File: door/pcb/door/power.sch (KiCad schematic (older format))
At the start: 6 parts, among them J1 USB_B_Micro, U1 LM1117-3.3

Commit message: caps voltage regulator gestauscht
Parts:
- removed C1: 10uF, Capacitor_SMD:C_0805_2012Metric, symbol Device:C
- removed C2: 100uF, Capacitor_SMD:C_0805_2012Metric, symbol Device:C
- added C1, C2: 10uF, Capacitor_Tantalum_SMD:CP_EIA-3216-10_Kemet-I, symbol Device:CP
- J1: footprint Connector_USB:USB_Micro-B_Amphenol_10103594-0001LF_Horizontal -> Connector_USB:USB_Micro-B_Wuerth_629105150521
- U1: value LM1117-3.3 -> 10uF
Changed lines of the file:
@@
 P 5050 3000
 F 0 "U1" H 5050 3242 50  0000 C CNN
-F 1 "LM1117-3.3" H 5050 3151 50  0000 C CNN
+F 1 "10uF" H 5050 3151 50  0000 C CNN
 F 2 "Package_TO_SOT_SMD:SOT-223" H 5050 3000 50  0001 C CNN
 F 3 "http://www.ti.com/lit/ds/symlink/lm1117.pdf" H 5050 3000 50  0001 C CNN
@@
 F 0 "J1" H 3655 3667 50  0000 C CNN
 F 1 "USB_B_Micro" H 3655 3576 50  0000 C CNN
-F 2 "Connector_USB:USB_Micro-B_Amphenol_10103594-0001LF_Horizontal" H 3750 3150 50  0001 C CNN
+F 2 "Connector_USB:USB_Micro-B_Wuerth_629105150521" H 3750 3150 50  0001 C CNN
 F 3 "~" H 3750 3150 50  0001 C CNN
 	1    3600 3200
@@
 	3900 3000 4000 3000
 Connection ~ 4150 3000
-$Comp
-L Device:C C1
-U 1 1 5BE81E66
-P 4600 3350
-F 0 "C1" H 4715 3396 50  0000 L CNN
-F 1 "10uF" H 4715 3305 50  0000 L CNN
-F 2 "Capacitor_SMD:C_0805_2012Metric" H 4638 3200 50  0001 C CNN
-F 3 "~" H 4600 3350 50  0001 C CNN
-	1    4600 3350
-	1    0    0    -1
-$EndComp
-$Comp
-L Device:C C2
-U 1 1 5BE81F8E
-P 5700 3350
-F 0 "C2" H 5815 3396 50  0000 L CNN
-F 1 "100uF" H 5815 3305 50  0000 L CNN
-F 2 "Capacitor_SMD:C_0805_2012Metric" H 5738 3200 50  0001 C CNN
-F 3 "~" H 5700 3350 50  0001 C CNN
-	1    5700 3350
-	1    0    0    -1
-$EndComp
 Wire Wire Line
 	4150 3000 4600 3000
@@
 Wire Wire Line
 	4000 3000 4150 3000
+$Comp
+L Device:CP C1
+U 1 1 5BF020CD
+P 4600 3350
+F 0 "C1" H 4718 3396 50  0000 L CNN
+F 1 "10uF" H 4718 3305 50  0000 L CNN
+F 2 "Capacitor_Tantalum_SMD:CP_EIA-3216-10_Kemet-I" H 4638 3200 50  0001 C CNN
+F 3 "~" H 4600 3350 50  0001 C CNN
+	1    4600 3350
+	1    0    0    -1
+$EndComp
+$Comp
+L Device:CP C2
+U 1 1 5BF021A6
+P 5700 3350
+F 0 "C2" H 5818 3396 50  0000 L CNN
+F 1 "10uF" H 5818 3305 50  0000 L CNN
+F 2 "Capacitor_Tantalum_SMD:CP_EIA-3216-10_Kemet-I" H 5738 3200 50  0001 C CNN
+F 3 "~" H 5700 3350 50  0001 C CNN
+	1    5700 3350
+	1    0    0    -1
+$EndComp
 $EndSCHEMATC

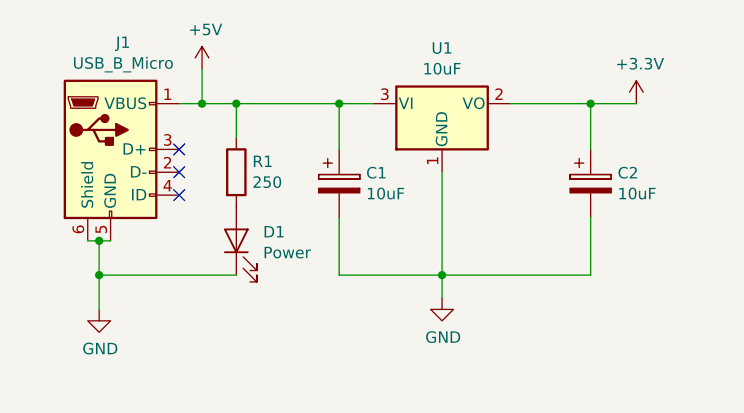
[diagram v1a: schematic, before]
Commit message: recplaced usb micro jack with barrel-jack, reworked pcb layout
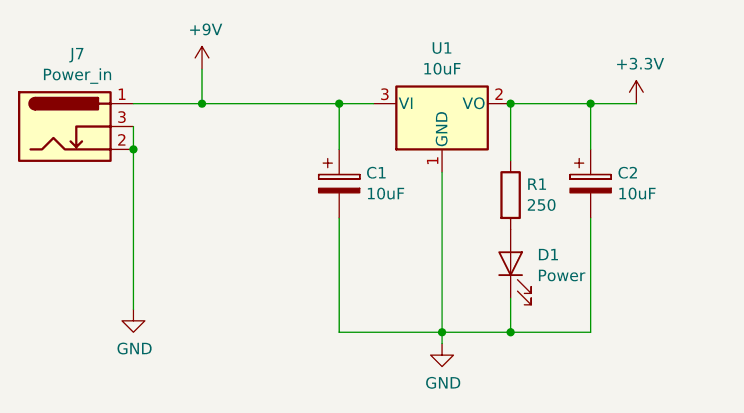
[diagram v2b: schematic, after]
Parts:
- removed J1: USB_B_Micro, Connector_USB:USB_Micro-B_Wuerth_629105150521, symbol Connector:USB_B_Micro
- added J7: Power_in, Connector_BarrelJack:BarrelJack_Wuerth_6941xx301002, symbol Connector:Barrel_Jack_Switch
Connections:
- net +3V3: now also R1.1
- net GND: now also J7.2, J7.3
- net +5V renamed +9V
- net +9V: now also J7.1; no longer R1.1
- no-connect marks 3 -> 0
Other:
- moved on the sheet: D1, R1
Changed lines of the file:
@@
 $EndComp
-$Comp
-L Connector:USB_B_Micro J1
-U 1 1 5BE809FE
-P 3600 3200
-F 0 "J1" H 3655 3667 50  0000 C CNN
-F 1 "USB_B_Micro" H 3655 3576 50  0000 C CNN
-F 2 "Connector_USB:USB_Micro-B_Wuerth_629105150521" H 3750 3150 50  0001 C CNN
-F 3 "~" H 3750 3150 50  0001 C CNN
-	1    3600 3200
-	1    0    0    -1
-$EndComp
-NoConn ~ 3900 3200
-NoConn ~ 3900 3300
-NoConn ~ 3900 3400
 $Comp
 L power:GND #PWR0101
 U 1 1 5BE80D93
-P 3550 3900
-F 0 "#PWR0101" H 3550 3650 50  0001 C CNN
-F 1 "GND" H 3555 3727 50  0000 C CNN
-F 2 "" H 3550 3900 50  0001 C CNN
-F 3 "" H 3550 3900 50  0001 C CNN
-	1    3550 3900
+P 3700 3900
+F 0 "#PWR0101" H 3700 3650 50  0001 C CNN
+F 1 "GND" H 3705 3727 50  0000 C CNN
+F 2 "" H 3700 3900 50  0001 C CNN
+F 3 "" H 3700 3900 50  0001 C CNN
+	1    3700 3900
 	1    0    0    -1
 $EndComp
-Wire Wire Line
-	3500 3600 3550 3600
-Connection ~ 3550 3600
-Wire Wire Line
-	3550 3600 3600 3600
 $Comp
 L power:+3.3V #PWR0102
@@
 L power:GND #PWR0103
 U 1 1 5BE80EEB
-P 5050 3850
-F 0 "#PWR0103" H 5050 3600 50  0001 C CNN
-F 1 "GND" H 5055 3677 50  0000 C CNN
-F 2 "" H 5050 3850 50  0001 C CNN
-F 3 "" H 5050 3850 50  0001 C CNN
-	1    5050 3850
+P 5050 4050
+F 0 "#PWR0103" H 5050 3800 50  0001 C CNN
+F 1 "GND" H 5055 3877 50  0000 C CNN
+F 2 "" H 5050 4050 50  0001 C CNN
+F 3 "" H 5050 4050 50  0001 C CNN
+	1    5050 4050
 	1    0    0    -1
 $EndComp
@@
 L Device:R R1
 U 1 1 5BE810F5
-P 4150 3300
-F 0 "R1" H 4220 3346 50  0000 L CNN
-F 1 "250" H 4220 3255 50  0000 L CNN
-F 2 "Resistor_SMD:R_0805_2012Metric" V 4080 3300 50  0001 C CNN
-F 3 "~" H 4150 3300 50  0001 C CNN
-	1    4150 3300
+P 5350 3400
+F 0 "R1" H 5420 3446 50  0000 L CNN
+F 1 "250" H 5420 3355 50  0000 L CNN
+F 2 "Resistor_SMD:R_0805_2012Metric" V 5280 3400 50  0001 C CNN
+F 3 "~" H 5350 3400 50  0001 C CNN
+	1    5350 3400
 	1    0    0    -1
 $EndComp
-Wire Wire Line
-	4150 3150 4150 3000
-Wire Wire Line
-	3900 3000 4000 3000
-Connection ~ 4150 3000
-Wire Wire Line
-	4150 3000 4600 3000
-Wire Wire Line
-	5050 3300 5050 3750
 Wire Wire Line
 	4600 3000 4600 3200
@@
 	4600 3000 4750 3000
 Wire Wire Line
-	4600 3500 4600 3750
-Wire Wire Line
-	4600 3750 5050 3750
-Connection ~ 5050 3750
-Wire Wire Line
-	5050 3750 5050 3850
-Wire Wire Line
 	5350 3000 5700 3000
 Wire Wire Line
 	5700 3000 5700 3200
 Wire Wire Line
-	5700 3500 5700 3750
-Wire Wire Line
-	5700 3750 5050 3750
-Wire Wire Line
 	5900 3000 5700 3000
 Connection ~ 5700 3000
-Wire Wire Line
-	3550 3600 3550 3750
 $Comp
 L Device:LED D1
 U 1 1 5BE80F7F
-P 4150 3600
-F 0 "D1" V 4188 3483 50  0000 R CNN
-F 1 "Power" V 4097 3483 50  0000 R CNN
-F 2 "LED_SMD:LED_1206_3216Metric" H 4150 3600 50  0001 C CNN
-F 3 "~" H 4150 3600 50  0001 C CNN
-	1    4150 3600
+P 5350 3700
+F 0 "D1" V 5388 3583 50  0000 R CNN
+F 1 "Power" V 5297 3583 50  0000 R CNN
+F 2 "LED_SMD:LED_1206_3216Metric" H 5350 3700 50  0001 C CNN
+F 3 "~" H 5350 3700 50  0001 C CNN
+	1    5350 3700
 	0    -1   -1   0
-$EndComp
-Wire Wire Line
-	4150 3750 3550 3750
-Connection ~ 3550 3750
-Wire Wire Line
-	3550 3750 3550 3900
-$Comp
-L power:+5V #PWR0111
-U 1 1 5BEBF68D
-P 4000 2850
-F 0 "#PWR0111" H 4000 2700 50  0001 C CNN
-F 1 "+5V" H 4015 3023 50  0000 C CNN
-F 2 "" H 4000 2850 50  0001 C CNN
-F 3 "" H 4000 2850 50  0001 C CNN
-	1    4000 2850
-	1    0    0    -1
 $EndComp
 Wire Wire Line
 	4000 2850 4000 3000
 Connection ~ 4000 3000
-Wire Wire Line
-	4000 3000 4150 3000
 $Comp
 L Device:CP C1
@@
 	1    0    0    -1
 $EndComp
+$Comp
+L Connector:Barrel_Jack_Switch J7
+U 1 1 5BFF06C7
+P 3400 3100
+F 0 "J7" H 3455 3417 50  0000 C CNN
+F 1 "Power_in" H 3455 3326 50  0000 C CNN
+F 2 "Connector_BarrelJack:BarrelJack_Wuerth_6941xx301002" H 3450 3060 50  0001 C CNN
+F 3 "~" H 3450 3060 50  0001 C CNN
+	1    3400 3100
+	1    0    0    -1
+$EndComp
+Wire Wire Line
+	3700 3000 4000 3000
+Wire Wire Line
+	3700 3100 3700 3200
+Connection ~ 3700 3200
+$Comp
+L power:+9V #PWR0111
+U 1 1 5BFF1461
+P 4000 2850
+F 0 "#PWR0111" H 4000 2700 50  0001 C CNN
+F 1 "+9V" H 4015 3023 50  0000 C CNN
+F 2 "" H 4000 2850 50  0001 C CNN
+F 3 "" H 4000 2850 50  0001 C CNN
+	1    4000 2850
+	1    0    0    -1
+$EndComp
+Wire Wire Line
+	4000 3000 4600 3000
+Wire Wire Line
+	3700 3200 3700 3900
+Wire Wire Line
+	4600 4000 5050 4000
+Wire Wire Line
+	4600 3500 4600 4000
+Connection ~ 5050 4000
+Wire Wire Line
+	5050 4000 5050 4050
+Wire Wire Line
+	5050 4000 5350 4000
+Wire Wire Line
+	5700 3500 5700 4000
+Wire Wire Line
+	5350 3850 5350 4000
+Connection ~ 5350 4000
+Wire Wire Line
+	5350 4000 5700 4000
+Wire Wire Line
+	5350 3250 5350 3000
+Connection ~ 5350 3000
+Wire Wire Line
+	5050 3300 5050 4000
 $EndSCHEMATC

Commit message: adjusted value of power led to 9V
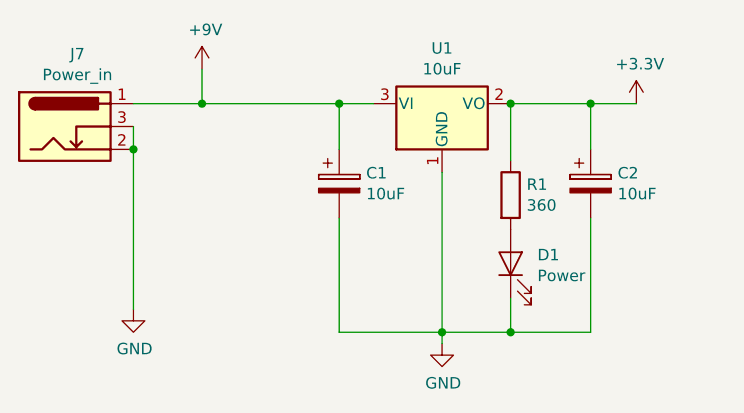
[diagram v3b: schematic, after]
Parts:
- R1: value 250 -> 360
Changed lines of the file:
@@
 P 5350 3400
 F 0 "R1" H 5420 3446 50  0000 L CNN
-F 1 "250" H 5420 3355 50  0000 L CNN
+F 1 "360" H 5420 3355 50  0000 L CNN
 F 2 "Resistor_SMD:R_0805_2012Metric" V 5280 3400 50  0001 C CNN
 F 3 "~" H 5350 3400 50  0001 C CNN

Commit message: reverse voltage protection added
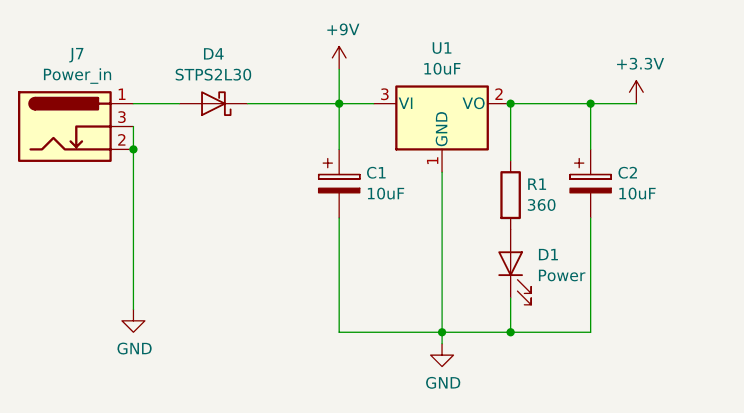
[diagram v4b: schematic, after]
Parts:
- added D4: STPS2L30, Diode_SMD:D_SMA, symbol Device:D_Schottky
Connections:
- net +9V: now also D4.1 (K); no longer J7.1
- new net: D4.2 (A), J7.1
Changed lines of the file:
@@
 $EndComp
 Wire Wire Line
-	4000 2850 4000 3000
-Connection ~ 4000 3000
+	4600 2850 4600 3000
 $Comp
 L Device:CP C1
@@
 	1    0    0    -1
 $EndComp
-Wire Wire Line
-	3700 3000 4000 3000
-Wire Wire Line
-	3700 3100 3700 3200
-Connection ~ 3700 3200
 $Comp
 L power:+9V #PWR0111
 U 1 1 5BFF1461
-P 4000 2850
-F 0 "#PWR0111" H 4000 2700 50  0001 C CNN
-F 1 "+9V" H 4015 3023 50  0000 C CNN
-F 2 "" H 4000 2850 50  0001 C CNN
-F 3 "" H 4000 2850 50  0001 C CNN
-	1    4000 2850
+P 4600 2850
+F 0 "#PWR0111" H 4600 2700 50  0001 C CNN
+F 1 "+9V" H 4615 3023 50  0000 C CNN
+F 2 "" H 4600 2850 50  0001 C CNN
+F 3 "" H 4600 2850 50  0001 C CNN
+	1    4600 2850
 	1    0    0    -1
 $EndComp
-Wire Wire Line
-	4000 3000 4600 3000
 Wire Wire Line
 	3700 3200 3700 3900
@@
 Wire Wire Line
 	5050 3300 5050 4000
+$Comp
+L Device:D_Schottky D4
+U 1 1 5C0443A7
+P 4050 3000
+F 0 "D4" H 4050 2784 50  0000 C CNN
+F 1 "STPS2L30" H 4050 2875 50  0000 C CNN
+F 2 "Diode_SMD:D_SMA" H 4050 3000 50  0001 C CNN
+F 3 "~" H 4050 3000 50  0001 C CNN
+	1    4050 3000
+	-1   0    0    1
+$EndComp
+Connection ~ 3700 3200
+Wire Wire Line
+	3700 3100 3700 3200
+Wire Wire Line
+	3700 3000 3900 3000
+Wire Wire Line
+	4200 3000 4600 3000
 $EndSCHEMATC

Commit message: changed pinout of DB-9 connector
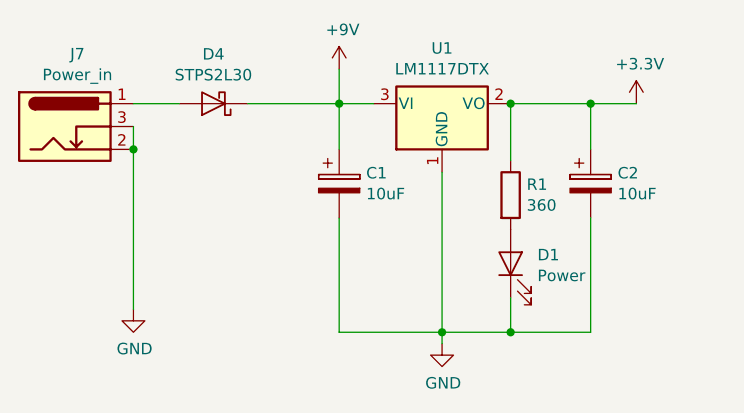
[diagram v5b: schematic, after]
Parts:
- U1: value 10uF -> LM1117DTX
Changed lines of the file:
@@
 P 5050 3000
 F 0 "U1" H 5050 3242 50  0000 C CNN
-F 1 "10uF" H 5050 3151 50  0000 C CNN
+F 1 "LM1117DTX" H 5050 3151 50  0000 C CNN
 F 2 "Package_TO_SOT_SMD:SOT-223" H 5050 3000 50  0001 C CNN
 F 3 "http://www.ti.com/lit/ds/symlink/lm1117.pdf" H 5050 3000 50  0001 C CNN
